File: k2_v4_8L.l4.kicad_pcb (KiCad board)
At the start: 8 copper layers, 120 x 46 mm, 42 parts, among them J11 J_EC_HEADER, J12 J_12V_IN, J13 J_SWD, J2 SlimSAS_x8_SFF8654, J3 MCIO_4i_SFF1016, J4 MCIO_4i_SFF1016, J6 J_PWR_CTRL, J9 J_OOB_HEADER, U1 STM32G0B1CBT6, U2 DCDC_12V_3V3, U4 BAT54C, U5 OPTO_LTV356T, U6 DS320PR1601

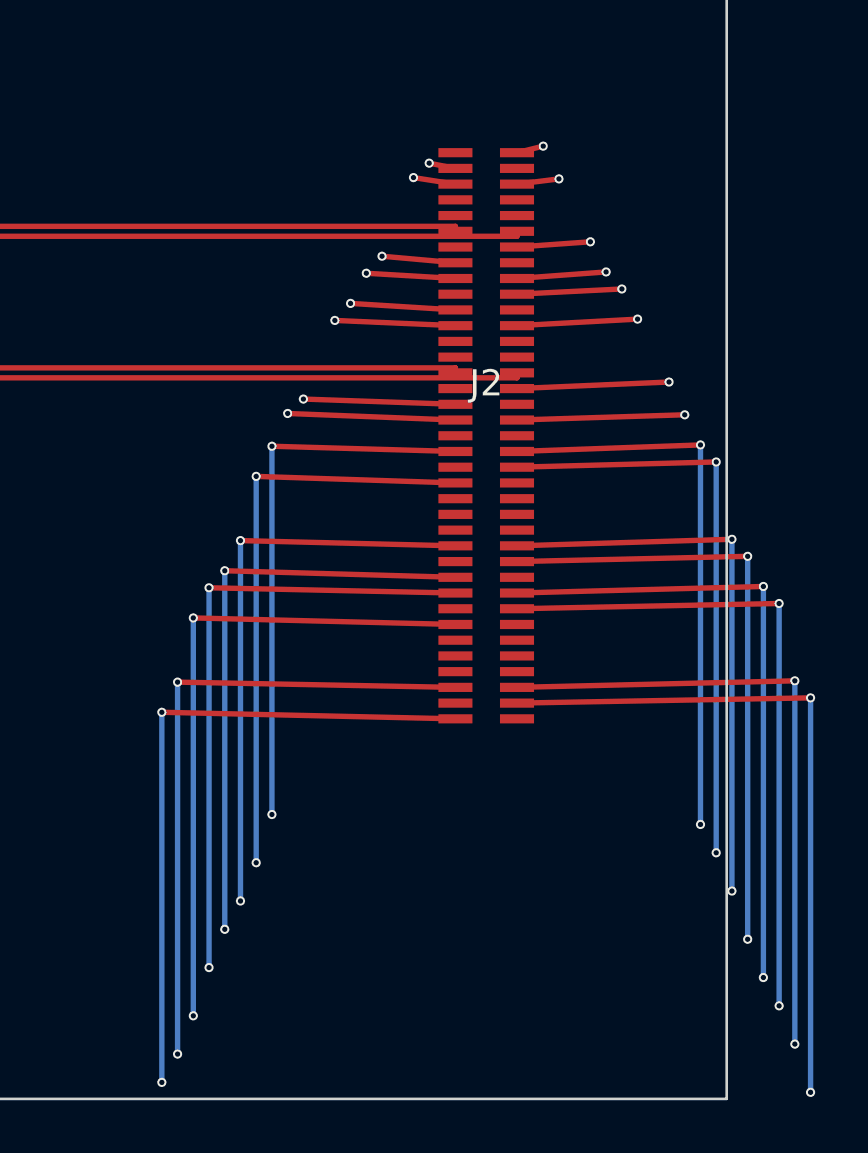
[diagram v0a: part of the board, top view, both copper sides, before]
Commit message: fix(k2): ROOT-22 — 解 R1/R2 耦合：成对落列 pitch 0.38→0.6(R3_STEP)
根因：CO-05b 成对落列 PAIR_PITCH=0.38 < max(VIA_VIA 0.525, VT_TRACK 0.4525)，
DN2/input land via(130.89,57.65) 与 UP1/out_J2 drop via(131.27,57.93) 相距 0.472，
逐页固定 ⇒ 该页全部 24234 pair_rows 被 _va 否决 ⇒ 回退无净距校核 phase-1
⇒ A-CN.1b/4/9。

修复：PAIR_PITCH=0.6(=R3_STEP)，band rank 不变 ⇒ 异列 Δx≥0.6 自动过 vv/vt；
同列 (DN_i,UP_i) via-y≥1.74 ⇒ W3 FEASIBLE_ALL。
副修：蛇形 node 发射 _mzp[1:-1]→[1:]（drop via 的 In2 顶点丢失，L4 曾丢 32 via）。

门控：G4/W3 PASS(main 05f7bd10ab3b45b6, 独立 A-CN.9 0/0/0, skew max 0.0574mm)
G5/W4 PASS(W3-VALv2.3, R3 重导纳入成对落列契约)
G6/L4 PASS(L4-A..E, 1710 段/256 via)
G7 OPEN：SI PASS(skew 0.0574)；DFM new=426 → CO-06(跨层过孔桶短路触 L2；D2..D6 L3 模型缺口)

L5 工具 8L 版本 bump + 新建 k2_v4_8L.kicad_pro(规则取自 drc_rules.json 语义)。
四源未改；未放宽 skew。
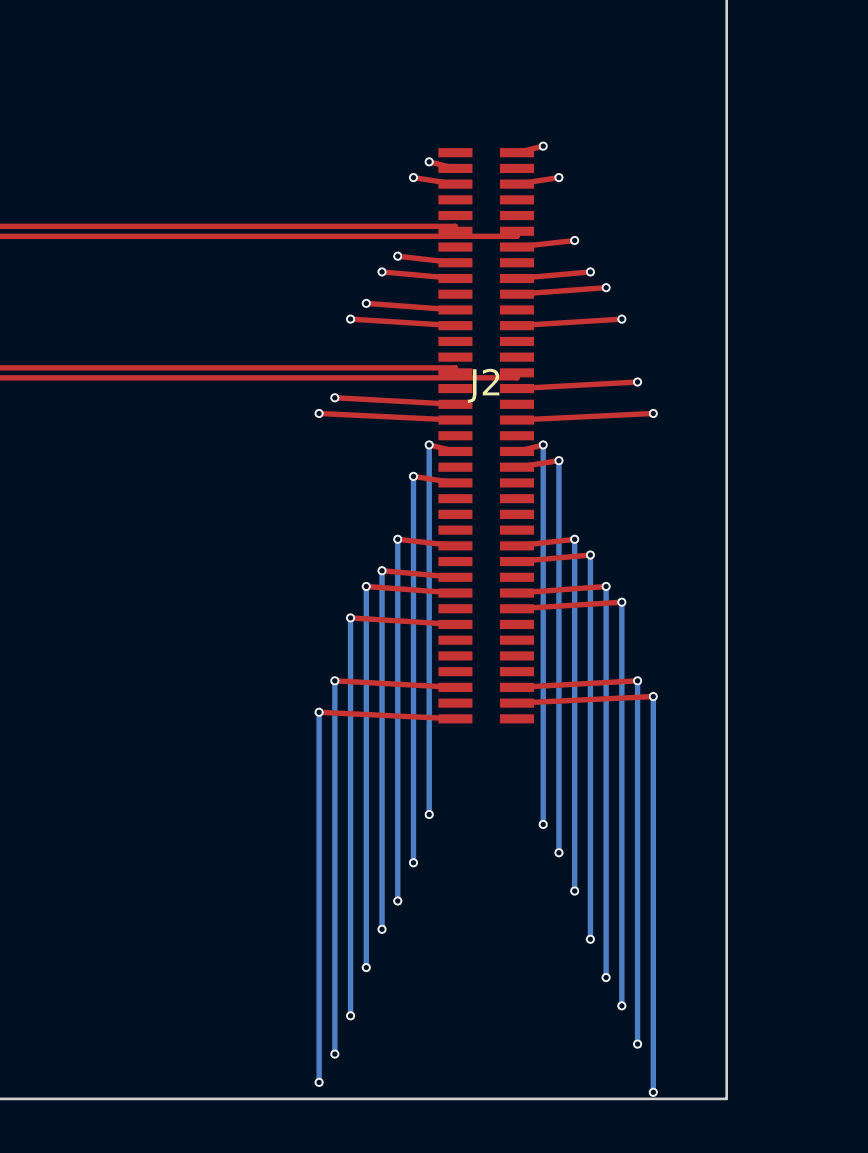
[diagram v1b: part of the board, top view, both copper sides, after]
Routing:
- net PCIE_UP_OUT7_P_J2: track 64.7 -> 77.9 mm
- net PCIE_DN7_N: track 75.4 -> 88.0 mm
- net PCIE_DN6_P: track 74.1 -> 86.5 mm
- net PCIE_DN6_N: track 98.5 -> 86.5 mm
- net PCIE_DN4_N: track 95.5 -> 83.5 mm
- net PCIE_DN2_N: track 92.2 -> 80.2 mm
- net PCIE_DN0_N: track 89.2 -> 77.2 mm
- net PCIE_DN7_P: track 100.0 -> 88.0 mm
- net PCIE_DN5_P: track 98.5 -> 86.5 mm
- net PCIE_DN3_P: track 93.7 -> 81.7 mm
- net PCIE_DN1_P: track 92.2 -> 80.3 mm
- net PCIE_UP_OUT6_N_J2: track 64.0 -> 75.7 mm
- net PCIE_DN5_N: track 74.8 -> 86.5 mm
- net PCIE_UP_OUT5_P_J2: track 64.8 -> 75.6 mm
- net PCIE_UP_OUT4_N_J2: track 64.2 -> 73.4 mm
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
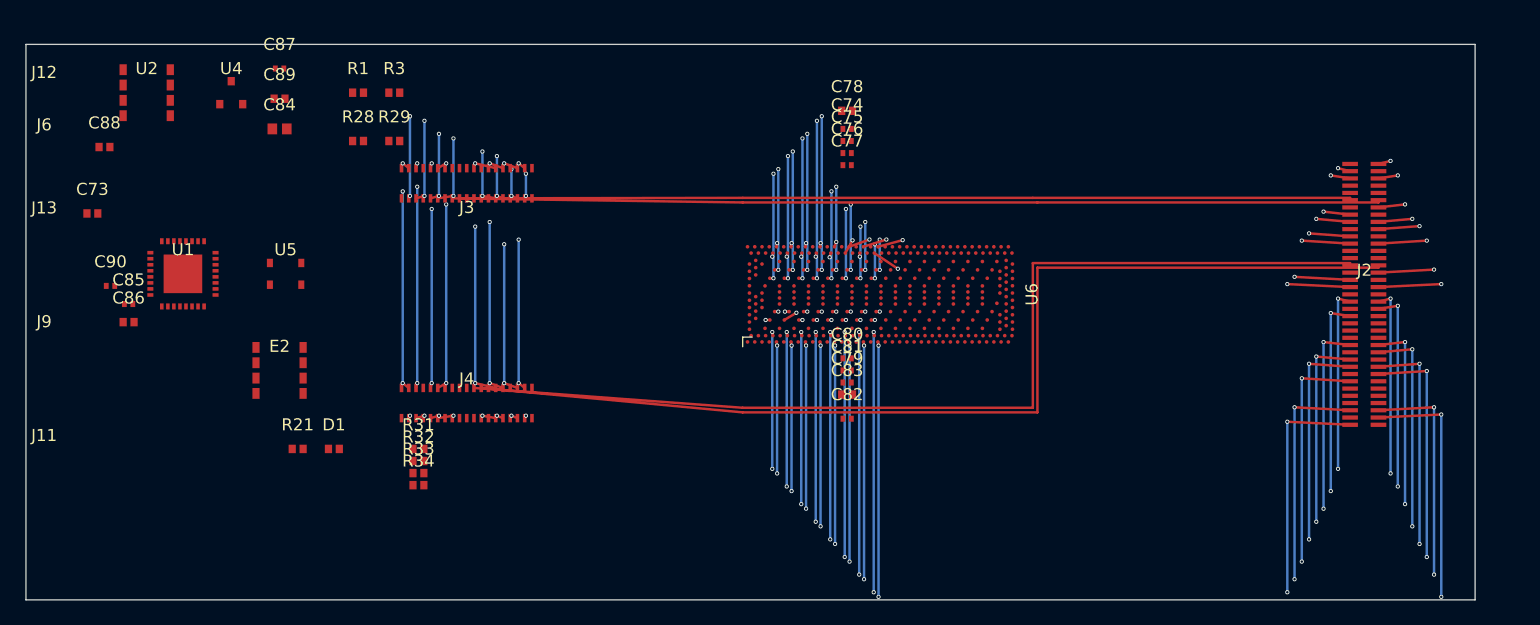
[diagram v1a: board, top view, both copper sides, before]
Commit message: CO-18: O4 有界幅值蛇形收口 -> 全板 FEASIBLE_ALL（W3-CN.34）；ECO SPEC-REV-2；G4/G5/G6 PASS
- 引擎 co16 路径：O4 等长蛇形改「vt 顶点净距限定幅值 + 浅齿闭式命中」
  A<=min(AMAX, Δy-vt)；a>=LEGSEP/2=0.19；teeth=ceil(extra/per_max) => 段长增量恰=extra
  30 条补偿线全部 lane-only 闭合（推翻 CO-17「几何不可行」= 45°-only 构造规则限定）
  canonical W3-CN.34 FEASIBLE_ALL cf60e9dd167e739c：certs=0 / crossings=0 / A-CN.9 0/0/0
  max|skew|=0.00306mm / 320 via / 三序逐字节 / wall 9.99s（AST while=0）
- ECO 同批：SPEC-REV-2 版本化新文件 0a7ad112ac4c57e3（原 SPEC 逐字节未动）+ 变更单
  引擎/验证器 FROZEN spec 同步；validator A1.3 max_vias_per_net 5->6
- 验证器 co16 口径（非豁免，CO-18 §4）：A1.2 按 shape 跑；A1.4 序取值按 shape；
  G-M4 增 co16 消费保真分支；A-CN.3c CO-16 扇面 y；via_min_inter 层跨不相交口径(span-blind 另记)；
  V5 走廊 run>=1mm（pad-access 微段=BGA 球距，L1）
- G6：L4 同点叠层 via 合并（CO-17 §4-2(D)）-> l4 板 248 via；L4-A..E PASS
- G7：SI PASS skew 0.0031；DFM new 426->103（holes_co_located 72->0）；残留 clearance/shorting/mask/edge 属 DFM 收口
- 裁定 m13_v57_CO18_o4_meander_bounded_amp_ruling.md 45ec35813344f7c5
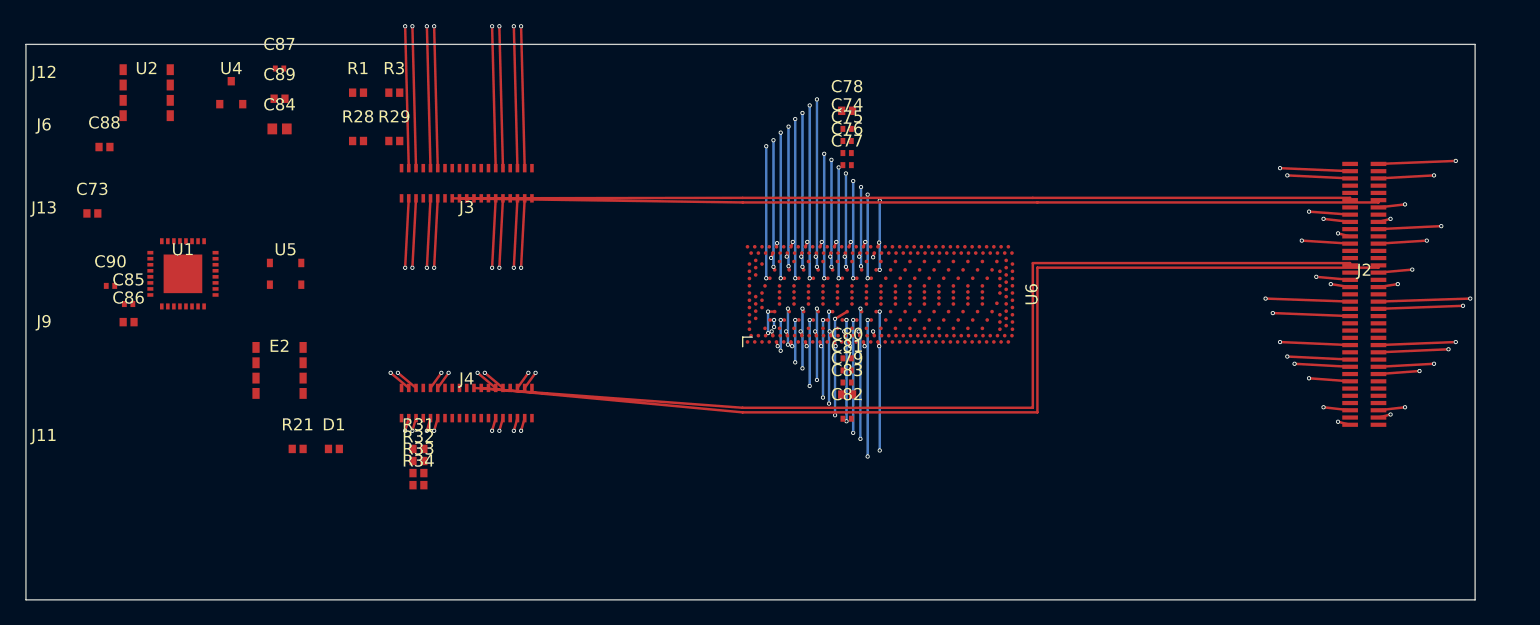
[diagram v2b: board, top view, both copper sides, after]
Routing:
- net PCIE_DN_OUT0_P_MCIO: track 33.5 -> 48.6 mm
- net PCIE_DN_OUT0_N_MCIO: track 33.5 -> 48.6 mm
- net PCIE_DN_OUT2_P_MCIO: track 47.9 -> 62.7 mm
- net PCIE_DN_OUT2_N_MCIO: track 47.9 -> 62.7 mm
- net PCIE_DN_OUT3_P_MCIO: track 53.9 -> 67.9 mm
- net PCIE_DN_OUT3_N_MCIO: track 53.9 -> 67.9 mm
- net PCIE_DN_OUT1_N_MCIO: track 40.6 -> 53.9 mm
- net PCIE_DN_OUT1_P_MCIO: track 40.6 -> 53.9 mm
- net PCIE_DN0_N: track 77.2 -> 90.5 mm
- net PCIE_DN0_P: track 77.2 -> 90.5 mm
- net PCIE_UP_OUT0_N_J2: track 67.2 -> 79.9 mm
- net PCIE_UP_OUT0_P_J2: track 67.2 -> 79.9 mm
- net PCIE_DN1_P: track 80.3 -> 92.1 mm
- net PCIE_DN1_N: track 80.3 -> 92.1 mm
- net PCIE_UP0_P: track 41.4 -> 52.7 mm
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
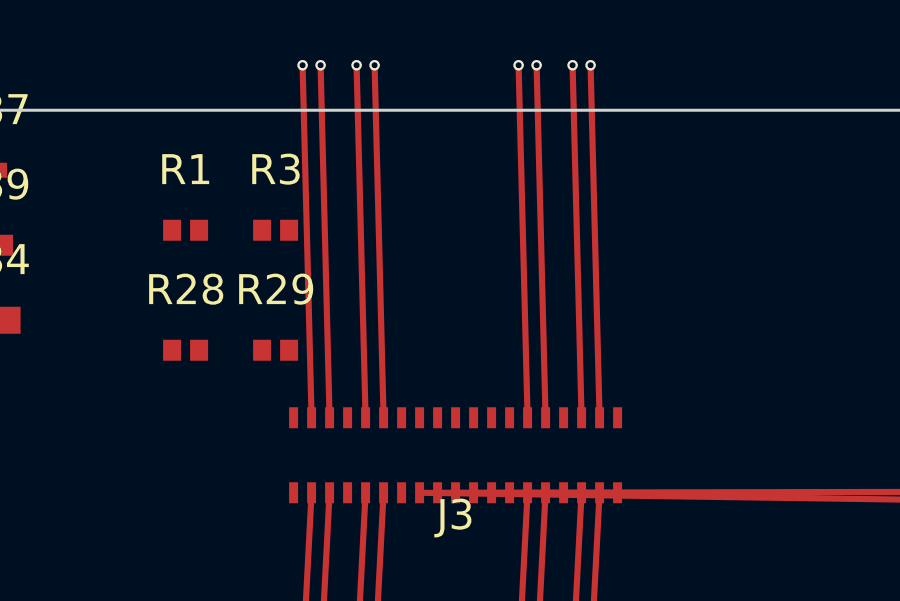
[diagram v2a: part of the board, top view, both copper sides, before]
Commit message: CO-19: CO16-ALLOC.2（板内 J3 fan）-> W3-CN.35 FEASIBLE_ALL（skew 0.00000）；DFM new 103->91 + 残留精确归因
- ALLOC.2：CO10_FANY_J3 31.5 -> 34.5,51.5（板 bbox y[32.95,79.05]，原值出板）；探针 32/32 + 独立复核 320/320 0 违规 PASS
  （emit 工具参数化：env 覆盖旋钮；默认仍逐字节复现 ALLOC.1 21ae78f8276d8df4）
- 引擎 W3-CN.35：CO16_ALLOC -> allocation_v2 + sha 236c72bc7d228fbf；FEASIBLE_ALL certs=0
  crossings 0/0、A-CN.9 0/0/0、320 via、max|skew| 0.00000mm、三序逐字节
- G4/G5/G6 PASS（validator W3-VALv2.3 PASS；L4 248 via、L4-A..E viol=0）
- G7 SI PASS（skew 0.0）；DFM new 426->91（tracks_crossing 1->0；copper_edge 29->14）
- 残留归因（CO-19 c8ffd4d0802591bc）：14=lane 平面超板边净空带（东跨度 45.76 > 可用 45.295；
  西最低 lane 33.05 < 需 33.3525）；3=同网 via 钻孔间距（PCIE_UP6/input N |lane_y-via1_y|=0.039）
  + 2 对同页 via；74=既有 PCIE_REFCLK0/1 路线与 J2/J3/J4/GND/P3V3 冲突（非 CO-16 拓扑）
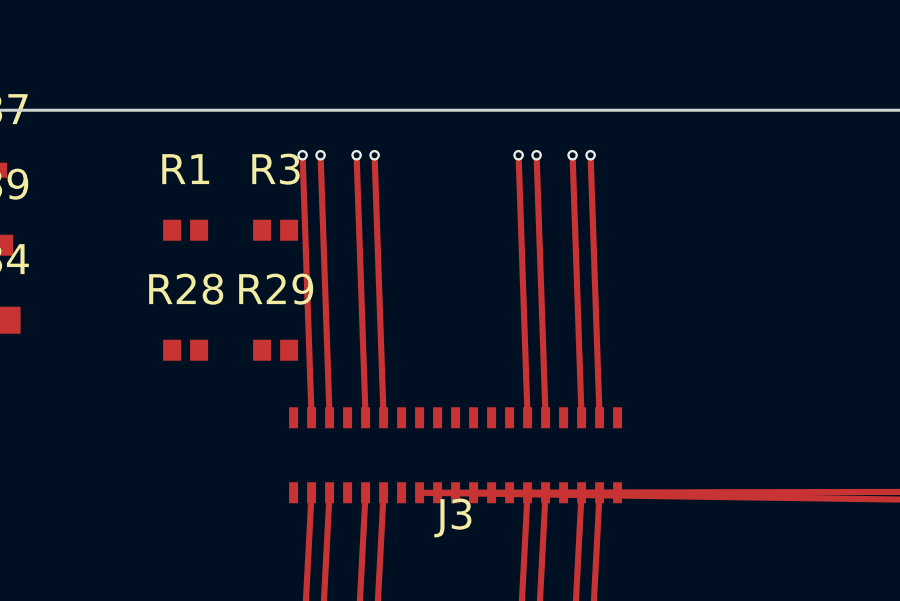
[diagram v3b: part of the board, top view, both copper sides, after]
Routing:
- net PCIE_UP1_N: track 55.5 -> 49.5 mm
- net PCIE_UP0_N: track 52.7 -> 46.7 mm
- net PCIE_UP0_P: track 52.7 -> 46.7 mm
- net PCIE_UP1_P: track 55.5 -> 49.5 mm
- net PCIE_UP2_N: track 61.5 -> 56.2 mm
- net PCIE_UP2_P: track 61.5 -> 56.2 mm
- net PCIE_UP3_N: track 64.5 -> 61.4 mm
- net PCIE_UP3_P: track 64.5 -> 61.4 mm

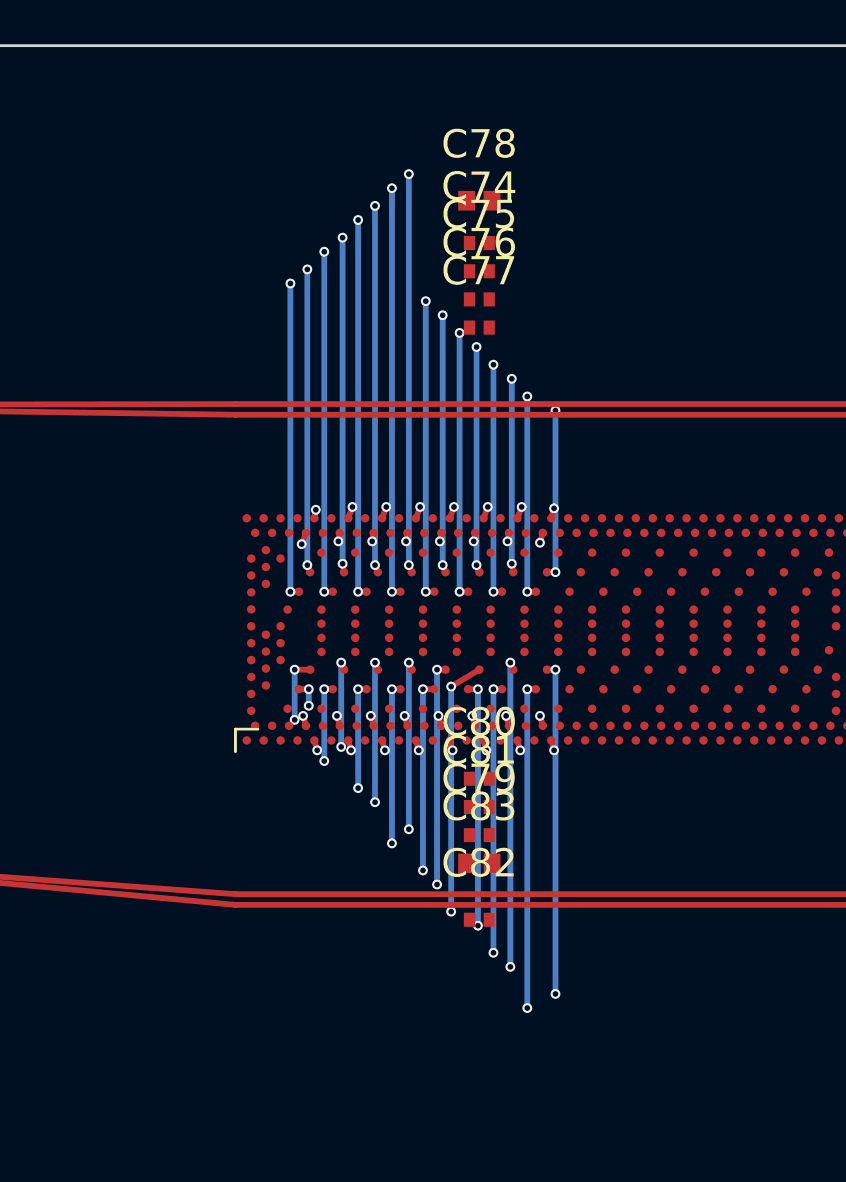
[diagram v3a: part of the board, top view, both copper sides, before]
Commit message: CO-22: lane 平面重整部分落地（CO16-ALLOC.3 / W3-CN.36, FEASIBLE_ALL skew 0.0031）；DFM 91->88 + 板边带标定更正
- ALLOC.3 238eb812a05eeac6：西 WLO 33.3->33.65、东 STEP 1.46->1.449 + 平移 -0.15（探针新旋钮 CO10_STEP/CO10_EDELTA/CO10_HOLE_GAP，默认中性）
  探针 32/32 + 独立复核 320/320 0 违规 PASS
- 引擎 W3-CN.36：FEASIBLE_ALL certs=0 / crossings 0 / A-CN.9 0/0/0 / 320 via / max|skew| 0.00306；新增板边带约束（蛇形顶点不出带）
- 板边标定更正：Edge.Cuts 实线 y=33.0/79.0（bbox 偏宽 0.05）=> lane 真带 [33.4025,78.5975]；真带下 STEP×EDELTA×4order 全扫无 32/32（最好 31/32）=> 东侧须 lane 带×stub/landing 同批重派生或 lane 索引置换
- L4-E 判据修正：两侧统一 0.1um 粒度（nm 往返噪声 ~1e-5）=> L4-A..E viol=0
- G4/G5/G6 PASS；G7 SI PASS(0.0031) / DFM FAIL new=88（copper_edge 14->12）
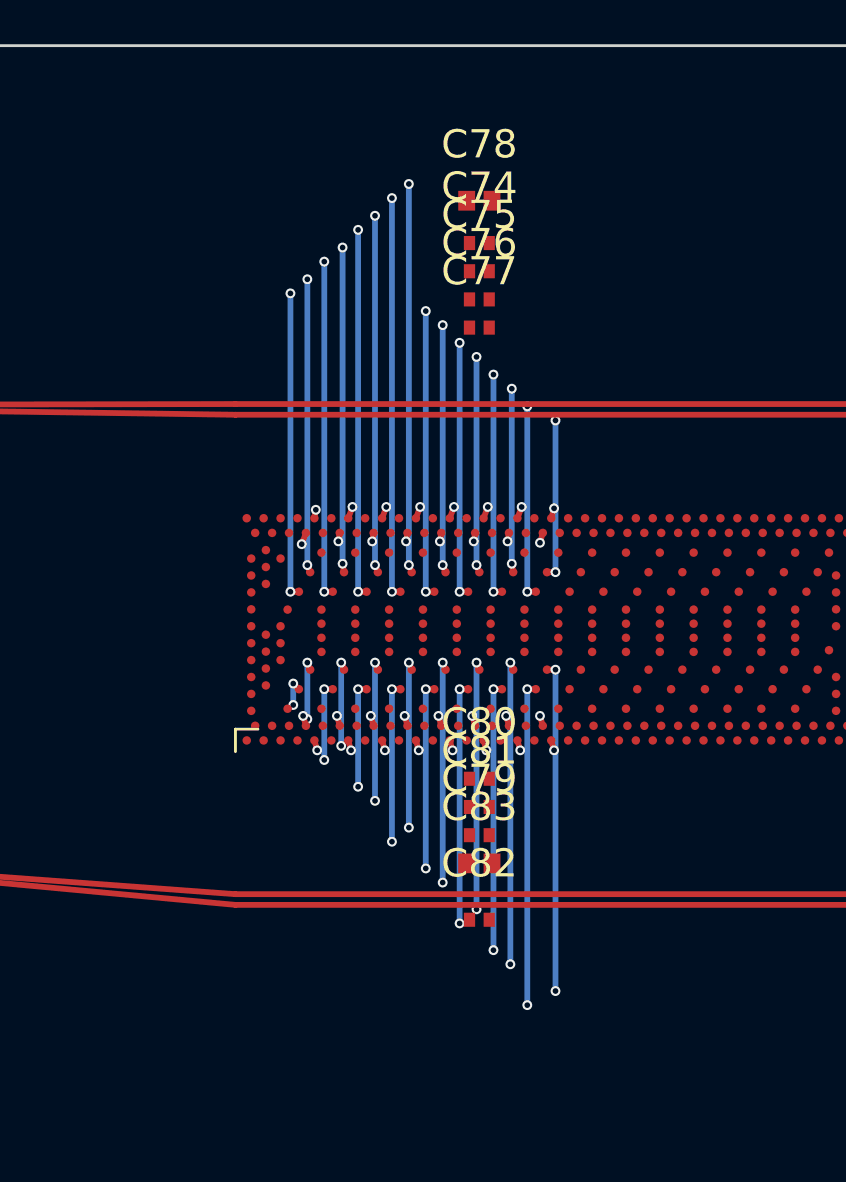
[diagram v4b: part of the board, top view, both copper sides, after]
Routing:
- net PCIE_UP3_P: track 61.4 -> 60.7 mm
- net PCIE_UP3_N: track 61.4 -> 60.7 mm
- net PCIE_UP5_N: track 55.6 -> 54.9 mm
- net PCIE_UP6_P: track 49.7 -> 49.0 mm
- net PCIE_UP5_P: track 55.6 -> 54.9 mm
- net PCIE_UP4_P: track 58.4 -> 57.7 mm
- net PCIE_DN_OUT7_P_MCIO: track 51.6 -> 50.9 mm
- net PCIE_DN_OUT7_N_MCIO: track 51.6 -> 50.9 mm
- net PCIE_DN_OUT6_P_MCIO: track 57.3 -> 56.6 mm
- net PCIE_DN_OUT6_N_MCIO: track 57.3 -> 56.6 mm
- net PCIE_DN_OUT5_P_MCIO: track 60.9 -> 60.2 mm
- net PCIE_DN_OUT5_N_MCIO: track 60.9 -> 60.2 mm
- net PCIE_DN_OUT4_N_MCIO: track 66.6 -> 65.9 mm
- net PCIE_DN_OUT3_N_MCIO: track 67.9 -> 67.2 mm
- net PCIE_DN_OUT2_N_MCIO: track 62.7 -> 62.0 mm
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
